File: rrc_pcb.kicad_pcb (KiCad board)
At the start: 2 copper layers, 143.9 x 68.6 mm, 20 parts, among them J1 Voltage Regulator Input, J2 Conn_01x03_Male, U1 ADXL357Z, U2 Teensy3.6-teensy, U3 BN220-GPS, U4 MS5611, U5 logo

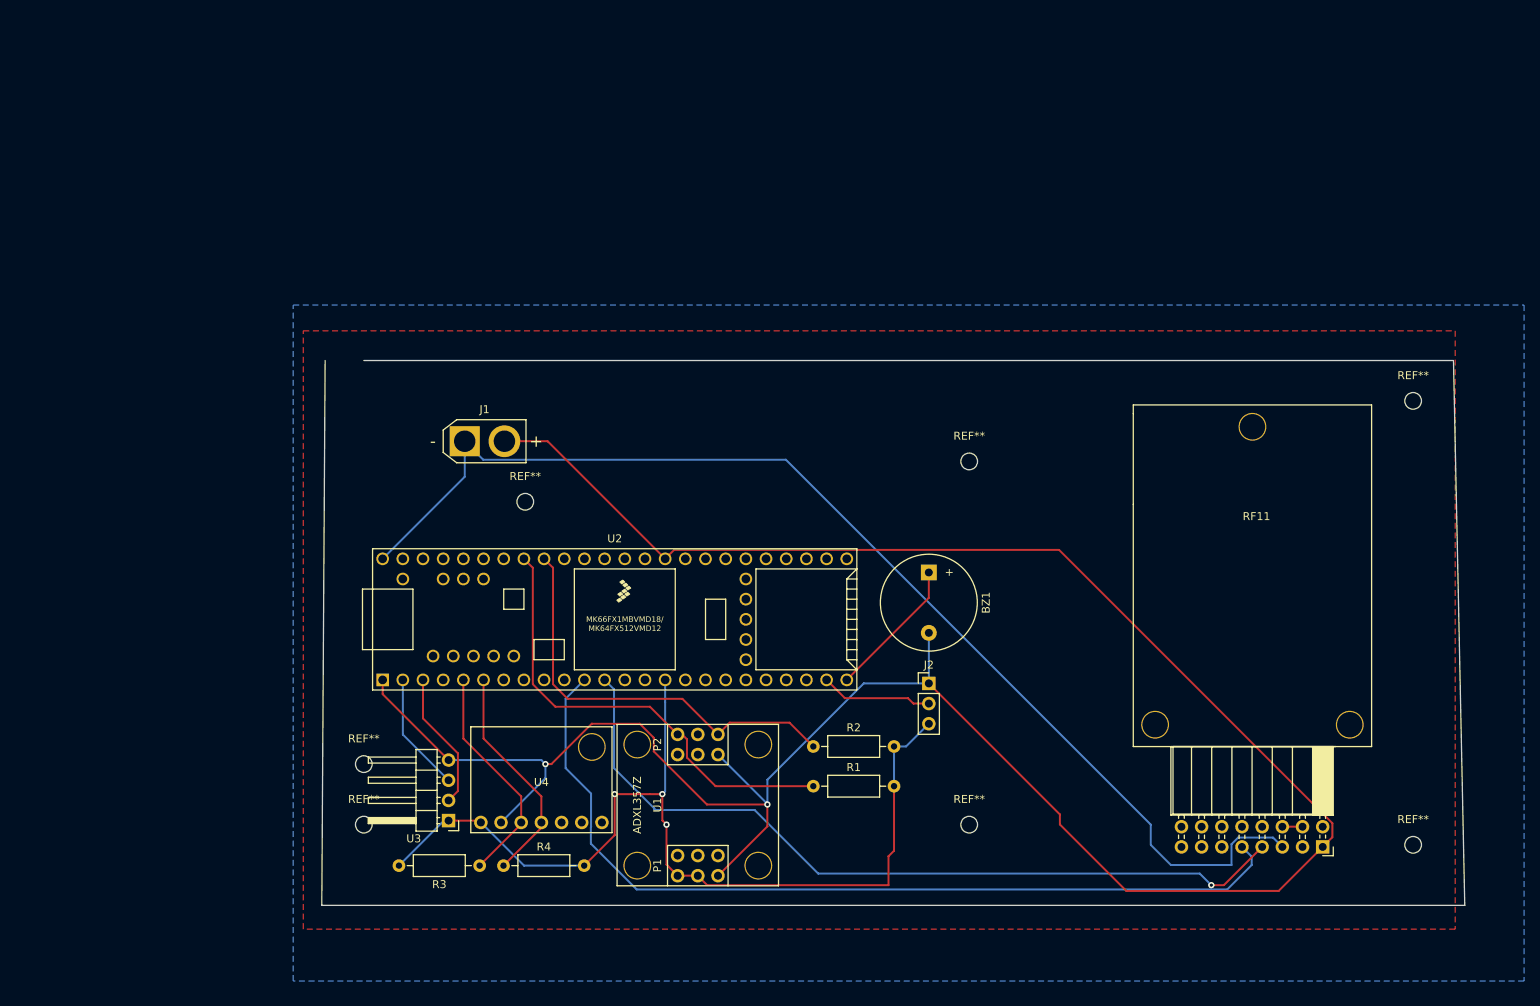
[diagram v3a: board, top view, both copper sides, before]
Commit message: fixed gps standoff points distances
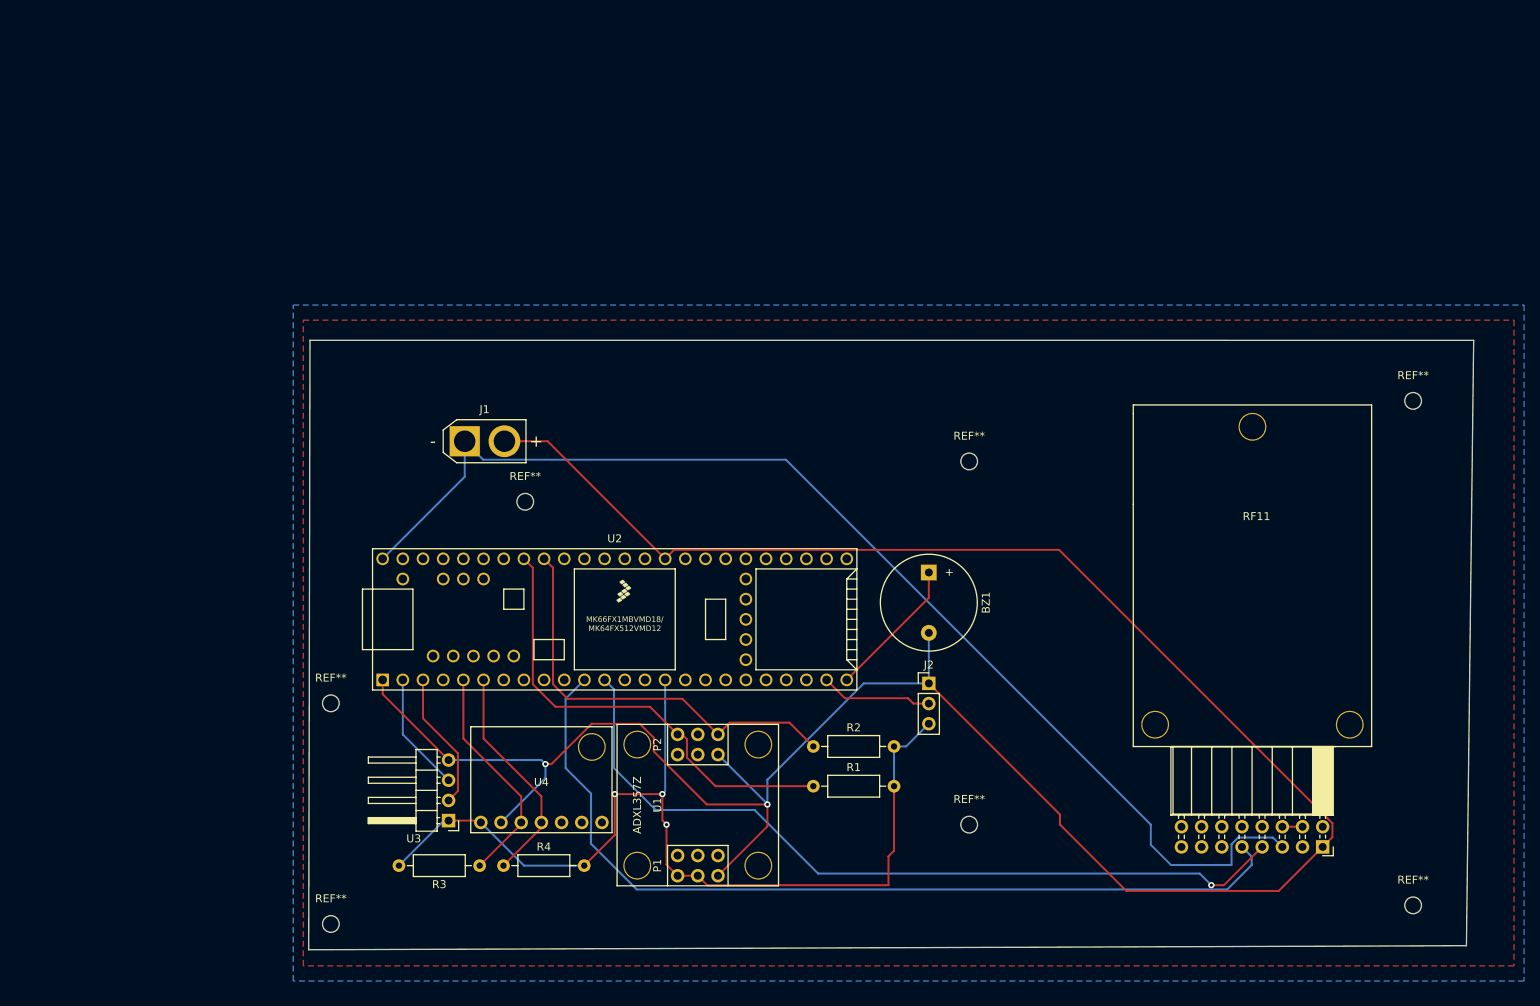
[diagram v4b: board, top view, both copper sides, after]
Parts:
- moved REF** 20.5 mm to (54.3, 129.3)
- moved REF** 15.8 mm to (54.3, 101.6)
- moved REF** 7.62 mm to (190.5, 127.0)
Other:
- board size 143.9 x 68.6 mm -> 146.6 x 76.7 mm
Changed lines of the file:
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@@
   )
   (footprint "MountingHole:MountingHole_2.1mm" (layer "F.Cu")
-    (at 58.42 116.84)
+    (at 54.270994 101.568447)
     (descr "Mounting Hole 2.1mm, no annular")
     (tags "mounting hole 2.1mm no annular")
@@
       (effects (font (size 1 1) (thickness 0.15)))
     )
-    (fp_text value "MountingHole_2.1mm" (at 0 3.2) (layer "F.Fab")
+    (fp_text value "MountingHole_2.1mm" (at -10.16 5.08) (layer "F.Fab")
       (effects (font (size 1 1) (thickness 0.15)))
     )
@@
   )
   (footprint "MountingHole:MountingHole_2.1mm" (layer "F.Cu")
-    (at 58.42 109.22)
+    (at 54.270994 129.345605)
     (descr "Mounting Hole 2.1mm, no annular")
     (tags "mounting hole 2.1mm no annular")
@@
   )
   (footprint "MountingHole:MountingHole_2.1mm" (layer "F.Cu")
-    (at 190.5 119.38)
+    (at 190.5 127)
     (descr "Mounting Hole 2.1mm, no annular")
     (tags "mounting hole 2.1mm no annular")
@@
       ) (layer "Eco2.User") (width 0.01) (fill solid))
   )
-  (gr_line (start 53.13 127) (end 53.55 58.42) (layer "Edge.Cuts") (width 0.05))
-  (gr_line (start 197 127) (end 53.13 127) (layer "Edge.Cuts") (width 0.05))
-  (gr_line (start 195.58 58.42) (end 197 127) (layer "Edge.Cuts") (width 0.05))
-  (gr_line (start 195.58 58.42) (end 58.42 58.42) (layer "Edge.Cuts") (width 0.05))
+  (gr_line (start 51.485154 132.589326) (end 51.645902 55.870288) (layer "Edge.Cuts") (width 0.05))
+  (gr_line (start 197.21 132.08) (end 51.485154 132.589326) (layer "Edge.Cuts") (width 0.05))
+  (gr_line (start 198.12 55.88) (end 197.21 132.08) (layer "Edge.Cuts") (width 0.05))
+  (gr_line (start 198.12 55.88) (end 51.645902 55.870288) (layer "Edge.Cuts") (width 0.05))
   (segment (start 76.12 68.58) (end 81.55 68.58) (width 0.25) (layer "F.Cu") (net 1))
   (segment (start 180.34 118.4207) (end 179.435119 119.325581) (width 0.25) (layer "F.Cu") (net 1))
@@
   (via (at 81.28 109.22) (size 0.8) (drill 0.4) (layers "F.Cu" "B.Cu") (free) (net 22))
   (via (at 109.22 114.3) (size 0.8) (drill 0.4) (layers "F.Cu" "B.Cu") (free) (net 22))
-  (segment (start 129.54 92.7) (end 129.54 99.06) (width 0.25) (layer "B.Cu") (net 22))
   (segment (start 75.692 116.566) (end 81.28 110.978) (width 0.25) (layer "B.Cu") (net 22))
   (segment (start 109.22 111.1897) (end 109.22 114.3) (width 0.25) (layer "B.Cu") (net 22))
@@
   (segment (start 129.54 99.06) (end 128.855489 99.744511) (width 0.25) (layer "B.Cu") (net 22))
   (segment (start 80.772 108.712) (end 81.28 109.22) (width 0.25) (layer "B.Cu") (net 22))
+  (segment (start 129.54 99.06) (end 129.54 92.7) (width 0.25) (layer "B.Cu") (net 22))
   (segment (start 109.22 114.3) (end 109.22 114.242) (width 0.25) (layer "B.Cu") (net 22))
   (segment (start 81.28 110.978) (end 81.28 109.22) (width 0.25) (layer "B.Cu") (net 22))
@@
     (polygon
       (pts
-        (xy 195.8 130)
-        (xy 50.8 130)
-        (xy 50.8 54.68)
-        (xy 195.8 54.68)
+        (xy 203.2 134.62)
+        (xy 50.8 134.62)
+        (xy 50.8 53.34)
+        (xy 203.2 53.34)
       )
     )

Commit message: fixed rfd location
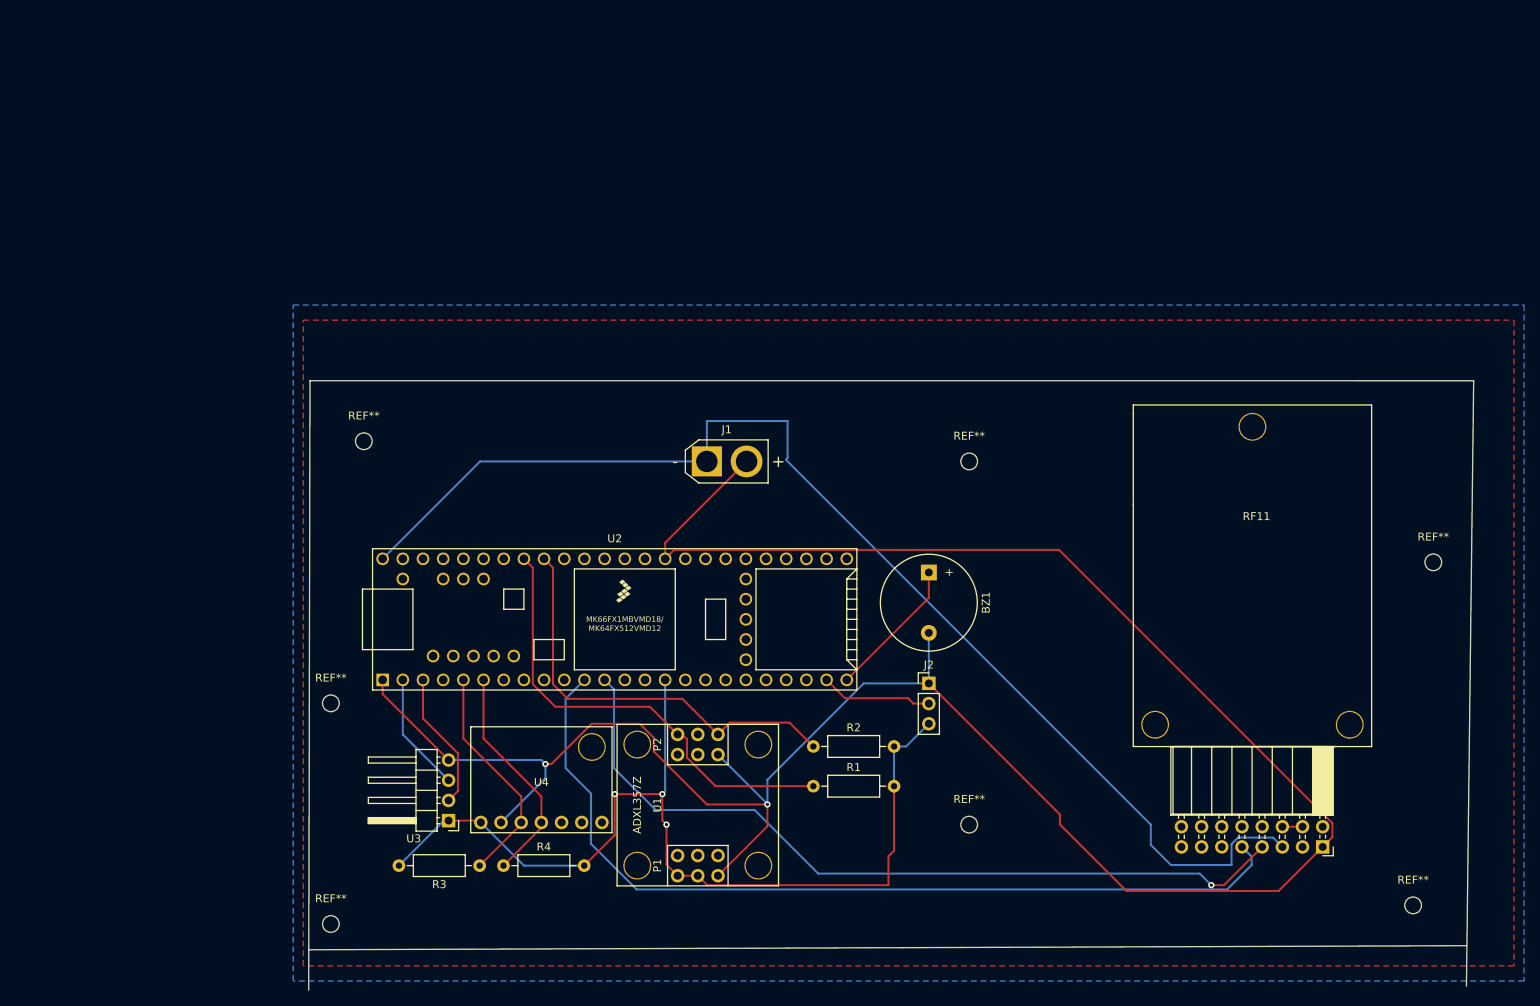
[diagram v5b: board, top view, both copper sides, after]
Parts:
- moved J1 30.6 mm to (101.6, 71.1)
- moved REF** 21.7 mm to (58.4, 68.6)
- moved REF** 20.5 mm to (193.0, 83.8)
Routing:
- net GND: track 128.2 -> 118.2 mm
- net VCC: track 149.0 -> 154.6 mm
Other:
- outline, holes or cut-outs redrawn
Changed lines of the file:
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@@
   )
   (footprint "Connector_AMASS:AMASS_XT30U-F_1x02_P5.0mm_Vertical" (layer "F.Cu")
-    (at 71.12 68.58)
+    (at 101.6 71.12)
     (descr "Connector XT30 Vertical Cable Female, https://www.tme.eu/en/Document/3cbfa5cfa544d79584972dd5234a409e/XT30U%20SPEC.pdf")
     (tags "RC Connector XT30")
@@
   )
   (footprint "MountingHole:MountingHole_2.1mm" (layer "F.Cu")
-    (at 78.74 76.2)
+    (at 58.42 68.58)
     (descr "Mounting Hole 2.1mm, no annular")
     (tags "mounting hole 2.1mm no annular")
@@
   )
   (footprint "MountingHole:MountingHole_2.1mm" (layer "F.Cu")
-    (at 190.5 63.5)
+    (at 193.04 83.82)
     (descr "Mounting Hole 2.1mm, no annular")
     (tags "mounting hole 2.1mm no annular")
@@
       ) (layer "Eco2.User") (width 0.01) (fill solid))
   )
-  (gr_line (start 51.485154 132.589326) (end 51.645902 55.870288) (layer "Edge.Cuts") (width 0.05))
+  (gr_line (start 51.485154 137.679038) (end 51.645902 60.96) (layer "Edge.Cuts") (width 0.05))
   (gr_line (start 197.21 132.08) (end 51.485154 132.589326) (layer "Edge.Cuts") (width 0.05))
-  (gr_line (start 198.12 55.88) (end 197.21 132.08) (layer "Edge.Cuts") (width 0.05))
-  (gr_line (start 198.12 55.88) (end 51.645902 55.870288) (layer "Edge.Cuts") (width 0.05))
-  (segment (start 76.12 68.58) (end 81.55 68.58) (width 0.25) (layer "F.Cu") (net 1))
+  (gr_line (start 198.12 60.969712) (end 197.21 137.169712) (layer "Edge.Cuts") (width 0.05))
+  (gr_line (start 198.12 60.969712) (end 51.645902 60.96) (layer "Edge.Cuts") (width 0.05))
   (segment (start 180.34 118.4207) (end 179.435119 119.325581) (width 0.25) (layer "F.Cu") (net 1))
+  (segment (start 96.35 81.37) (end 96.35 83.38) (width 0.25) (layer "F.Cu") (net 1))
   (segment (start 180.34 116.66517) (end 180.34 118.4207) (width 0.25) (layer "F.Cu") (net 1))
   (segment (start 96.35 83.38) (end 97.474511 82.255489) (width 0.25) (layer "F.Cu") (net 1))
   (segment (start 97.474511 82.255489) (end 145.930319 82.255489) (width 0.25) (layer "F.Cu") (net 1))
+  (segment (start 106.6 71.12) (end 96.35 81.37) (width 0.25) (layer "F.Cu") (net 1))
   (segment (start 145.930319 82.255489) (end 180.34 116.66517) (width 0.25) (layer "F.Cu") (net 1))
-  (segment (start 81.55 68.58) (end 96.35 83.38) (width 0.25) (layer "F.Cu") (net 1))
-  (segment (start 76.12 68.58) (end 76.2 68.58) (width 0.25) (layer "B.Cu") (net 1))
-  (segment (start 71.12 73.05) (end 60.79 83.38) (width 0.25) (layer "B.Cu") (net 2))
+  (segment (start 101.6 66.04) (end 111.76 66.04) (width 0.25) (layer "B.Cu") (net 2))
   (segment (start 167.64 121.92) (end 167.64 119.29969) (width 0.25) (layer "B.Cu") (net 2))
   (segment (start 172.862749 118.468929) (end 174.03726 119.64344) (width 0.25) (layer "B.Cu") (net 2))
+  (segment (start 111.76 66.04) (end 111.76 70.689022) (width 0.25) (layer "B.Cu") (net 2))
+  (segment (start 101.6 71.12) (end 73.05 71.12) (width 0.25) (layer "B.Cu") (net 2))
   (segment (start 168.470761 118.468929) (end 172.862749 118.468929) (width 0.25) (layer "B.Cu") (net 2))
-  (segment (start 71.12 68.58) (end 73.444511 70.904511) (width 0.25) (layer "B.Cu") (net 2))
+  (segment (start 111.76 70.689022) (end 111.544511 70.904511) (width 0.25) (layer "B.Cu") (net 2))
   (segment (start 157.48 119.38) (end 160.02 121.92) (width 0.25) (layer "B.Cu") (net 2))
+  (segment (start 101.6 71.12) (end 101.6 66.04) (width 0.25) (layer "B.Cu") (net 2))
   (segment (start 157.48 116.84) (end 157.48 119.38) (width 0.25) (layer "B.Cu") (net 2))
-  (segment (start 73.444511 70.904511) (end 111.544511 70.904511) (width 0.25) (layer "B.Cu") (net 2))
   (segment (start 167.64 119.29969) (end 168.470761 118.468929) (width 0.25) (layer "B.Cu") (net 2))
-  (segment (start 71.12 68.58) (end 71.12 73.05) (width 0.25) (layer "B.Cu") (net 2))
   (segment (start 160.02 121.92) (end 167.64 121.92) (width 0.25) (layer "B.Cu") (net 2))
+  (segment (start 73.05 71.12) (end 60.79 83.38) (width 0.25) (layer "B.Cu") (net 2))
   (segment (start 111.544511 70.904511) (end 157.48 116.84) (width 0.25) (layer "B.Cu") (net 2))
   (segment (start 90 113) (end 94.469002 113) (width 0.25) (layer "F.Cu") (net 3))

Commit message: fixed pcb and changed layout
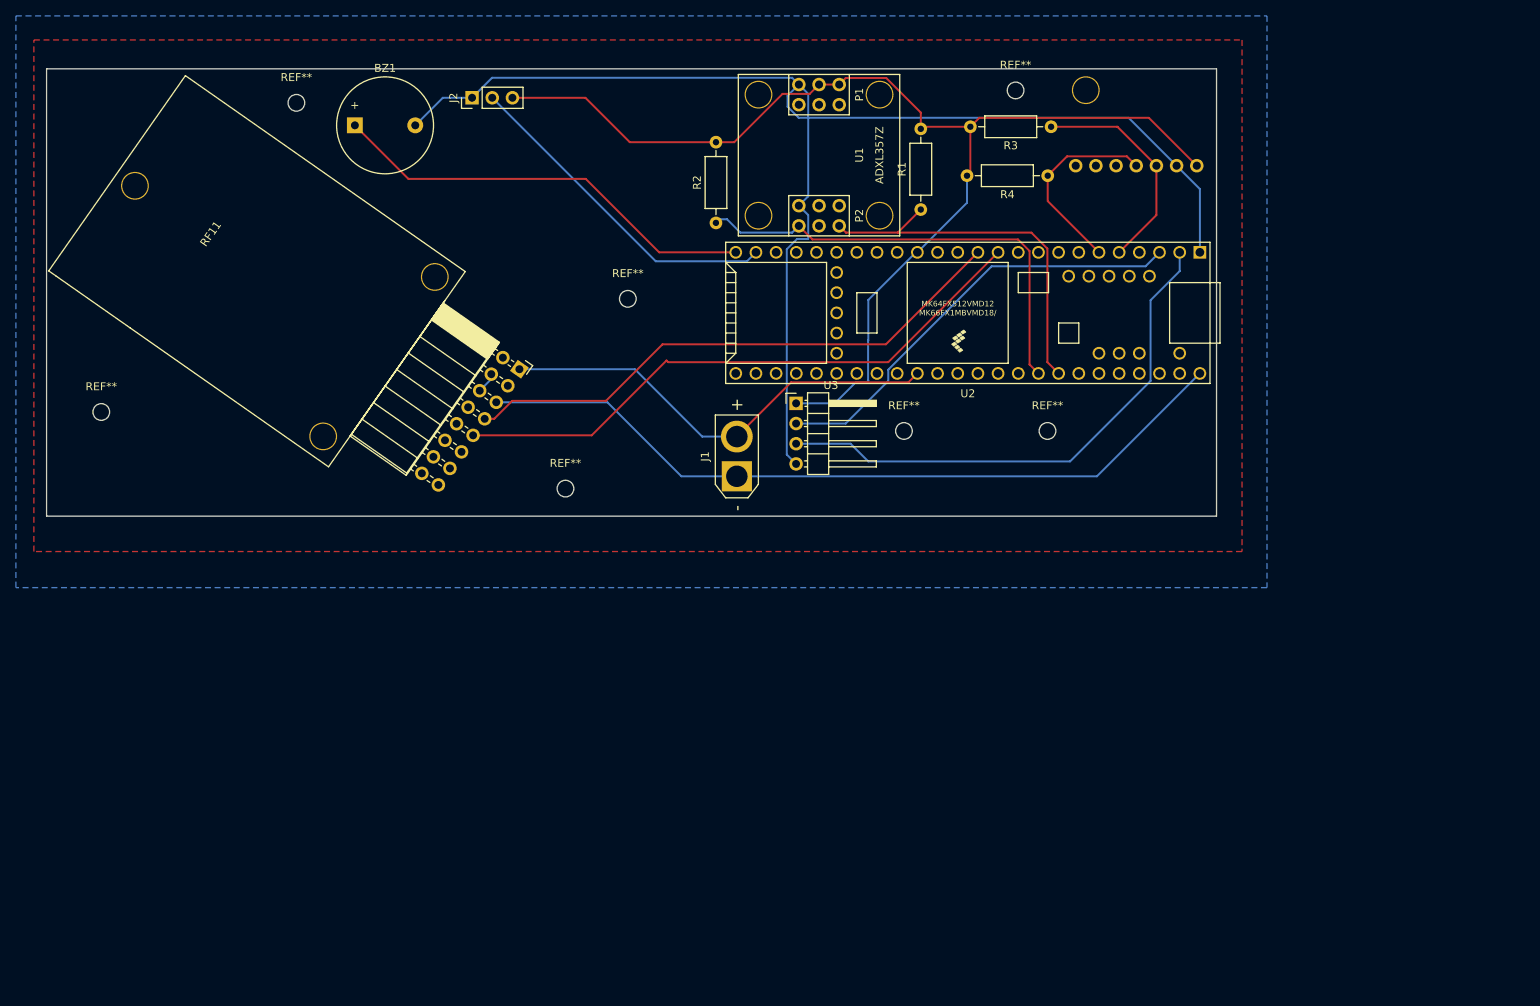
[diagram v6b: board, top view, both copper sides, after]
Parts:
- removed the REF** at (134.6, 116.8)
- removed the REF** at (58.4, 68.6)
- removed the REF** at (54.3, 129.3)
- removed the REF** at (193.0, 83.8)
- removed the REF** at (134.6, 71.1)
- removed the REF** at (190.5, 127.0)
- added REF**: MountingHole_2.1mm, MountingHole:MountingHole_2.1mm, F.Cu at (25.4, 64.9)
- added REF**: MountingHole_2.1mm, MountingHole:MountingHole_2.1mm, F.Cu at (126.4, 67.3)
- added REF**: MountingHole_2.1mm, MountingHole:MountingHole_2.1mm, F.Cu at (83.8, 74.5)
- added REF**: MountingHole_2.1mm, MountingHole:MountingHole_2.1mm, F.Cu at (140.5, 24.4)
- added REF**: MountingHole_2.1mm, MountingHole:MountingHole_2.1mm, F.Cu at (144.5, 67.3)
- added REF**: MountingHole_2.1mm, MountingHole:MountingHole_2.1mm, F.Cu at (91.7, 50.7)
- U4: moved to B.Cu
- moved U5 129.4 mm to (45.7, 48.3), turned to 55 degrees
- moved R3 117.6 mm to (144.9, 29.0)
- moved U4 111.5 mm to (155.6, 37.7), turned to 180 degrees
- moved R4 110.6 mm to (144.5, 35.2), turned to 180 degrees
- moved RF11 107.2 mm to (54.0, 71.8), turned to 55 degrees
- moved U1 97.6 mm to (113.2, 25.0), turned to -90 degrees
- moved J2 93.5 mm to (72.0, 25.3), turned to 90 degrees
- moved BZ1 91.6 mm to (57.3, 28.8), turned to 0 degrees
- moved REF** 75.7 mm to (49.9, 26.0)
- moved R1 73.8 mm to (128.5, 39.4), turned to 90 degrees
- moved U3 68.4 mm to (112.8, 63.8), turned to 0 degrees
- moved R2 67.0 mm to (102.7, 41.1), turned to 90 degrees
- moved U2 58.9 mm to (134.4, 52.4), turned to 180 degrees
- moved J1 4.21 mm to (105.4, 73.0), turned to 90 degrees
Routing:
- net GND: track 118.2 -> 56.9 mm
- net VCC: track 154.6 -> 97.8 mm
- net Net-(U2-Pad2): track 15.0 -> 67.4 mm
- net Net-(U2-Pad3): track 17.5 -> 55.5 mm
- net Net-(BZ1-Pad1): track 17.8 -> 54.6 mm
- net Net-(RF11-Pad9): track 112.6 -> 75.8 mm
- net Net-(RF11-Pad7): track 101.5 -> 70.8 mm, vias 1 -> 0
- net Net-(J2-Pad2): track 14.1 -> 42.2 mm
- net T_VCC: track 120.9 -> 146.4 mm, vias 3 -> 0
- net T_GND: track 191.4 -> 170.3 mm, vias 2 -> 0
- net Net-(R1-Pad1): track 58.2 -> 47.8 mm
- net Net-(R2-Pad1): track 53.5 -> 57.9 mm
- net Net-(R4-Pad1): track 29.1 -> 25.0 mm
- net Net-(R3-Pad1): track 29.0 -> 28.1 mm
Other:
- board size 146.6 x 76.7 mm -> 147.3 x 56.3 mm
